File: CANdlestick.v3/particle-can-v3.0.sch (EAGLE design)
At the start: 11 parts, among them IC1 LM2940, IC2 TJA1049, J1 OBDII

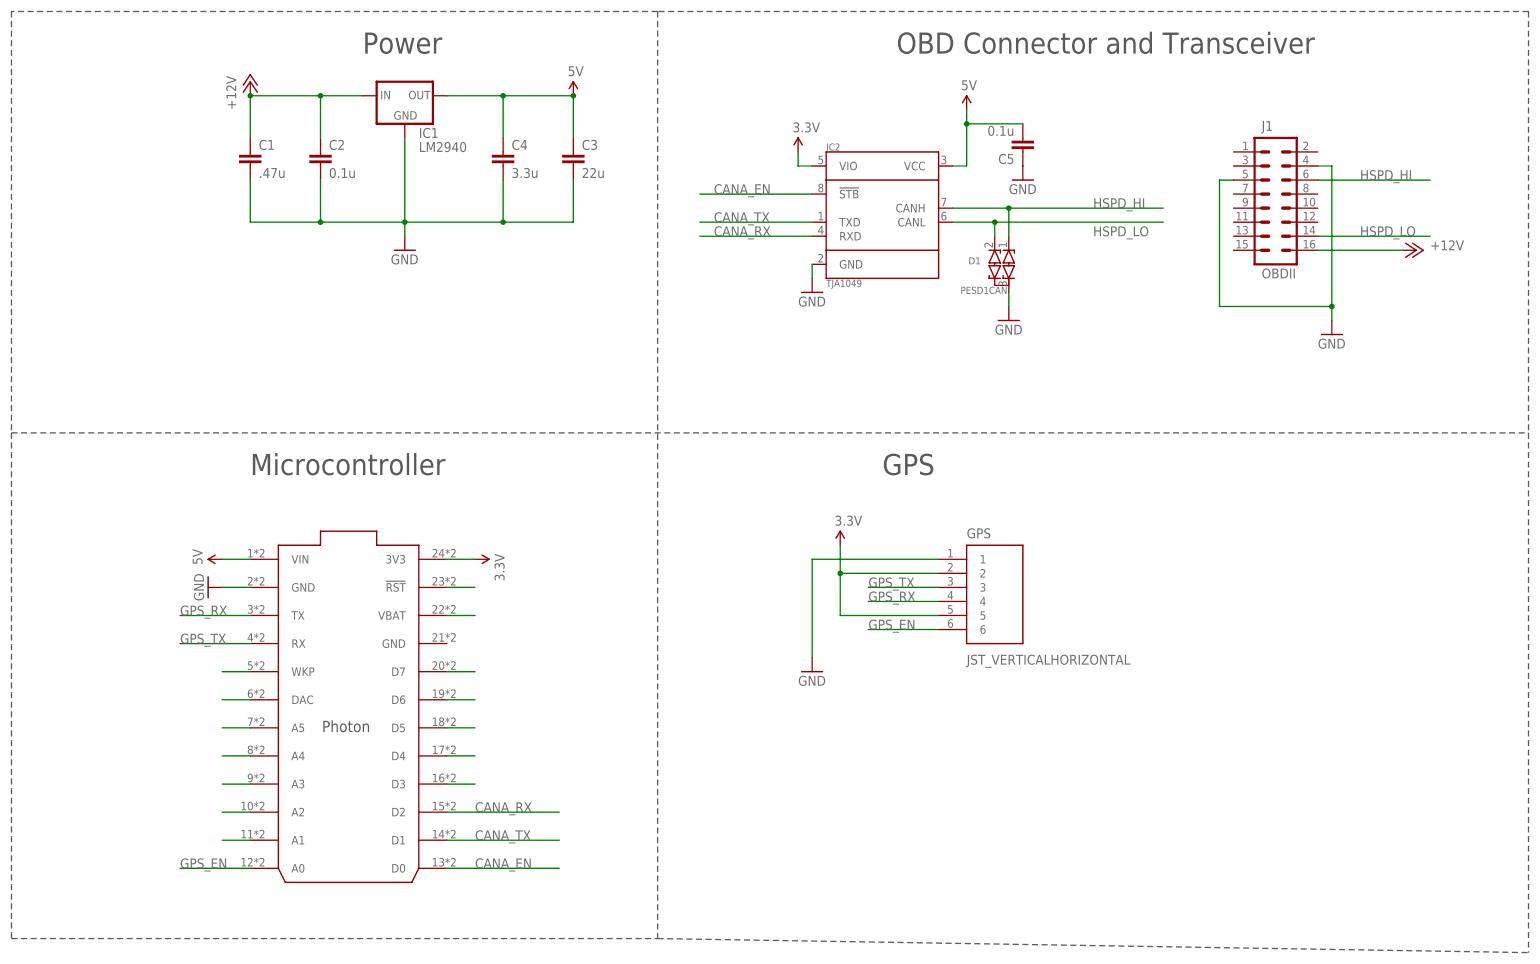
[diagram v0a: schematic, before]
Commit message: Revision 3 has the PCB extending outward and SD card
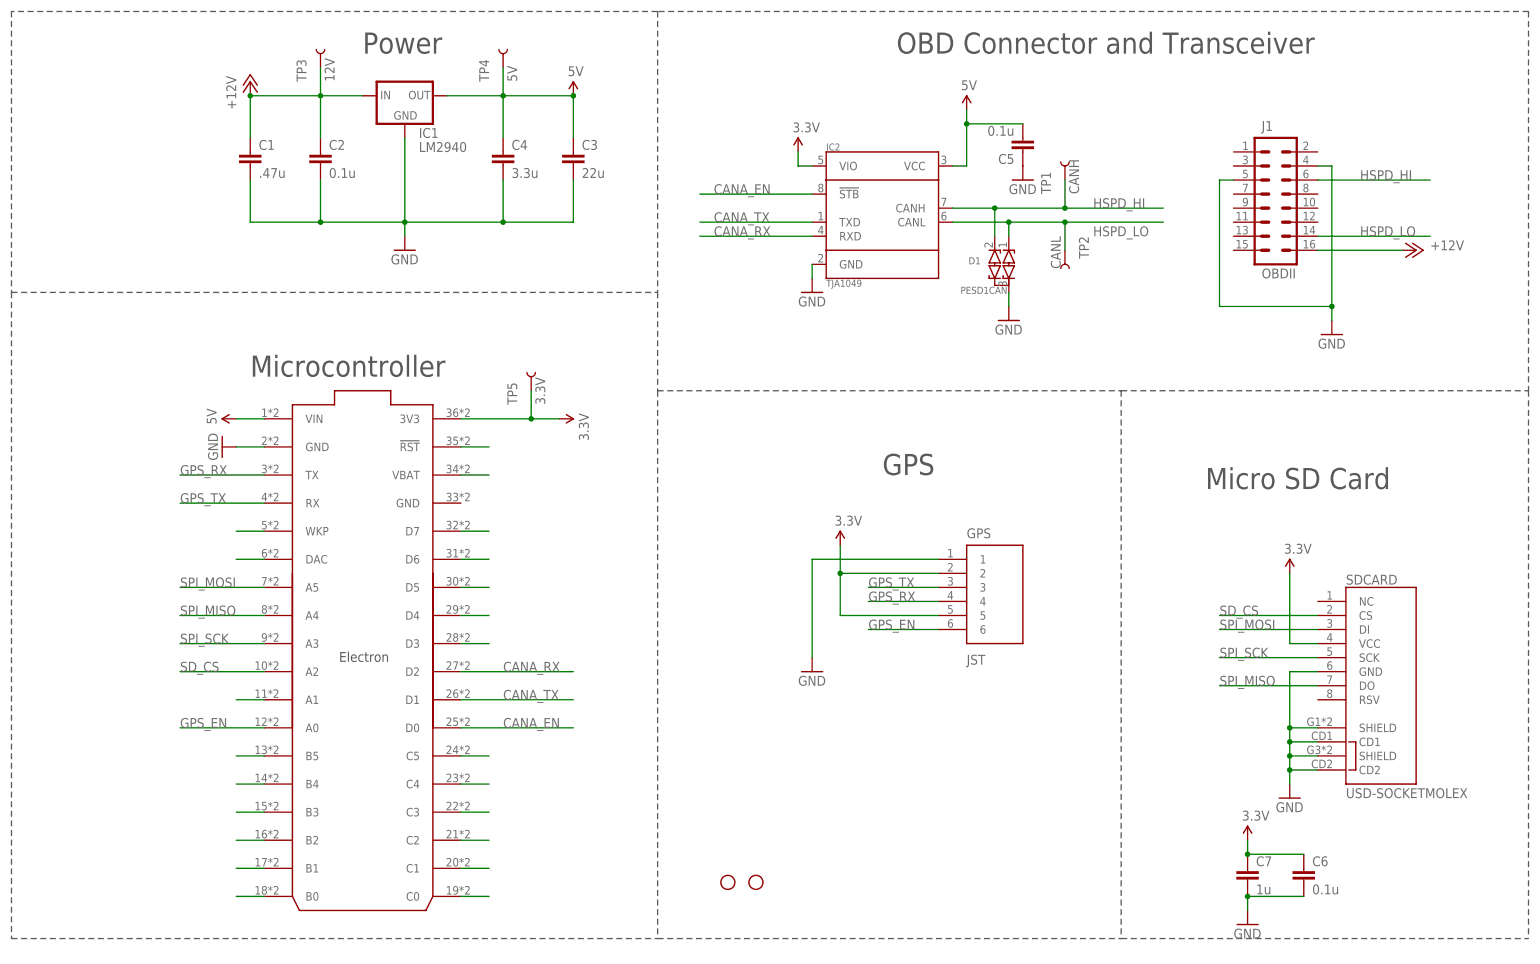
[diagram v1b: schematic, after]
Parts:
- removed CORE: PHOTONWITH_EXTERNAL_HEADERS, MuniRent:PHOTONWITH_EXTERNAL_HEADERS
- added C6: 0.1u, rcl:C-EUC0805
- added C7: 1u, rcl:C-EUC0805
- added ELECTRON: ELECTRON_WITH_EXTERNAL_HEADERS, MuniRent:ELECTRON_WITH_EXTERNAL_HEADERS
- added SDCARD: USD-SOCKETMOLEX, MuniRent:USD-SOCKETMOLEX
- added STANDOFF1, STANDOFF2: STAND-OFF, SparkFun-Electromechanical:STAND-OFF
- added TP1: CANH, SparkFun-Passives:TEST-POINT3
- added TP2: CANL, SparkFun-Passives:TEST-POINT3
- added TP3: 12V, SparkFun-Passives:TEST-POINT3
- added TP4: 5V, SparkFun-Passives:TEST-POINT3
- added TP5: 3.3V, SparkFun-Passives:TEST-POINT3
- GPS: value JST_VERTICALHORIZONTAL -> JST; device MuniRent:JST_VERTICALHORIZONTAL -> MuniRent:JST; PARTNO JST-6-HOR -> BM06B-SRSS-TB
- J1: device MuniRent:M08X2STRAIGHT -> MuniRent:M08X2-OBDII-COMTECH
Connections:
- new net N$1: ELECTRON.B5
- new net N$17: ELECTRON.B3
- new net N$21: ELECTRON.B0
- new net N$22: ELECTRON.C0
- new net N$27: ELECTRON.C4
- new net N$28: ELECTRON.C5
- new net N$29: ELECTRON.C3
- new net N$7: ELECTRON.B4
- new net SD_CS: ELECTRON.A2, SDCARD.CS
- new net SPI_MISO: ELECTRON.A4, SDCARD.DO
- new net SPI_MOSI: ELECTRON.A5, SDCARD.DI
- new net SPI_SCK: ELECTRON.A3, SDCARD.SCK
- net +12V: now also TP3.1
- net 3.3V: now also C6.1, C7.1, ELECTRON.3V3, SDCARD.VCC, TP5.1; no longer CORE.3V3
- net 5V: now also ELECTRON.VIN, TP4.1; no longer CORE.VIN
- net CANA_EN: now also ELECTRON.D0; no longer CORE.D0
- net CANA_RX: now also ELECTRON.D2; no longer CORE.D2
- net CANA_TX: now also ELECTRON.D1; no longer CORE.D1
- net GND: now also C6.2, C7.2, ELECTRON.GND@2, SDCARD.CD1, SDCARD.CD2, SDCARD.GND, SDCARD.SHIELD@1, SDCARD.SHIELD@3; no longer CORE.GND@2
- net GPS_EN: now also ELECTRON.A0; no longer CORE.A0
- net GPS_RX: now also ELECTRON.TX; no longer CORE.TX
- net GPS_TX: now also ELECTRON.RX; no longer CORE.RX
- net HSPD_HI: now also D1.C2, TP1.1; no longer D1.C1
- net HSPD_LO: now also D1.C1, TP2.1; no longer D1.C2
- net N$10: now also ELECTRON.!RST; no longer CORE.!RST
- net N$11: now also ELECTRON.VBAT; no longer CORE.VBAT
- net N$12: now also ELECTRON.D7; no longer CORE.D7
- net N$13: now also ELECTRON.D6; no longer CORE.D6
- net N$14: now also ELECTRON.D5; no longer CORE.D5
- net N$15: now also ELECTRON.D4; no longer CORE.D4
- net N$16: now also ELECTRON.D3; no longer CORE.D3
- net N$18: now also ELECTRON.A1; no longer CORE.A1
- net N$19: now also ELECTRON.B2; no longer CORE.A2
- net N$20: now also ELECTRON.B1; no longer CORE.A3
- net N$23: now also ELECTRON.C1; no longer CORE.A4
- net N$24: now also ELECTRON.C2; no longer CORE.A5
- net N$25: now also ELECTRON.DAC; no longer CORE.DAC
- net N$26: now also ELECTRON.WKP; no longer CORE.WKP
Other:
- note added: "Micro SD Card"

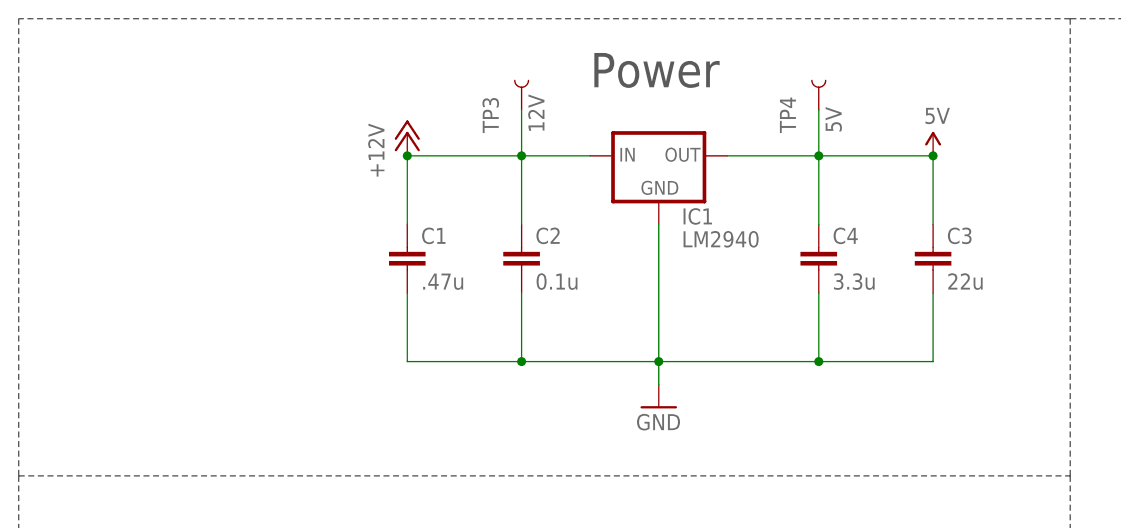
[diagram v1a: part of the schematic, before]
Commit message: Revision 3 grows outward (different form factor)
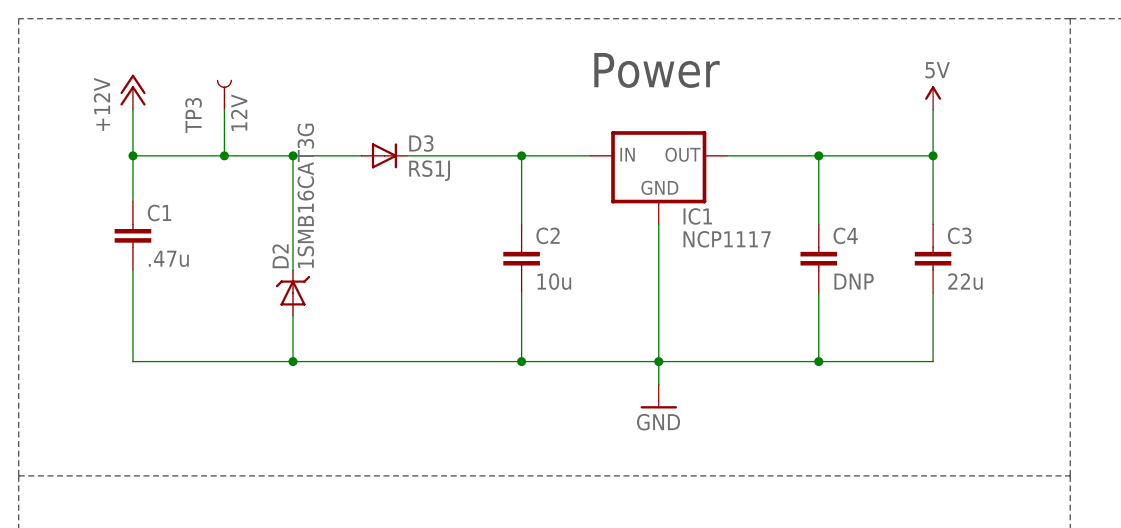
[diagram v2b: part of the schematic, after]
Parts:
- removed TP4: 5V, SparkFun-Passives:TEST-POINT3
- added D2: 1SMB16CAT3G, BUG:DIODE-TVS-SMB
- added D3: RS1J, BUG:DIODESMA
- C2: value 0.1u -> 10u; PARTNO 08055C104KAT2A -> GRM21BR6YA106KE43L
- C4: value 3.3u -> DNP; PARTNO C0805C335K8PACTU -> GRM219R61A226MEA0D
- IC1: value LM2940 -> NCP1117; device MuniRent:LM2940 -> MuniRent:NCP1117; PARTNO LM2940IMP-5.0/NOPB -> NCP1117LPST50T3G
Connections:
- new net N$31: C2.1, D3.C, IC1.IN
- net +12V: now also D2.C, D3.A; no longer C2.1, IC1.IN
- net 5V: no longer TP4.1
- net GND: now also D2.A
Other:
- moved on the sheet: C1, TP3
